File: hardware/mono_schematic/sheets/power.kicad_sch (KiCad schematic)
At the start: 37 parts

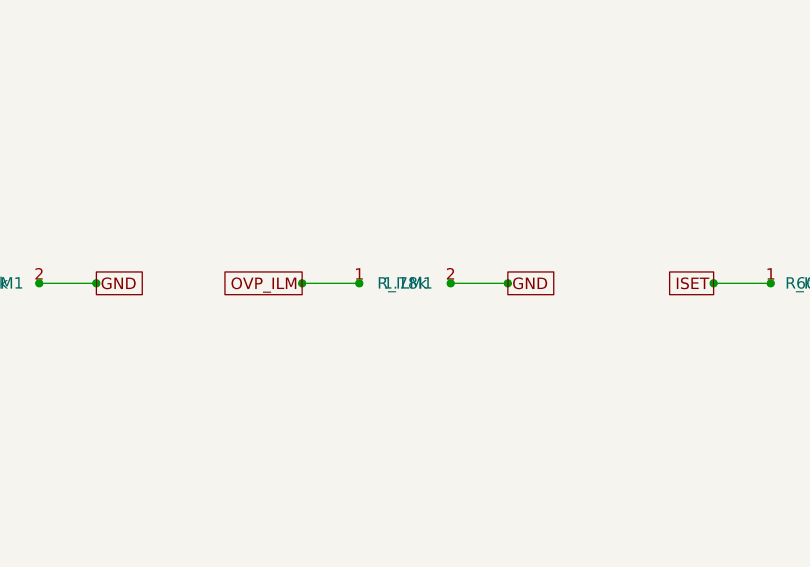
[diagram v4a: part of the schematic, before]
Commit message: mono_electronics v13 chunk4: abs-max review of every part; R_ILM1 1.78k->2.7k (eFuse limit 0.79 A < BQ25185 1.1 A IN abs max); schematic regen (ERC 0, 0 diffs)
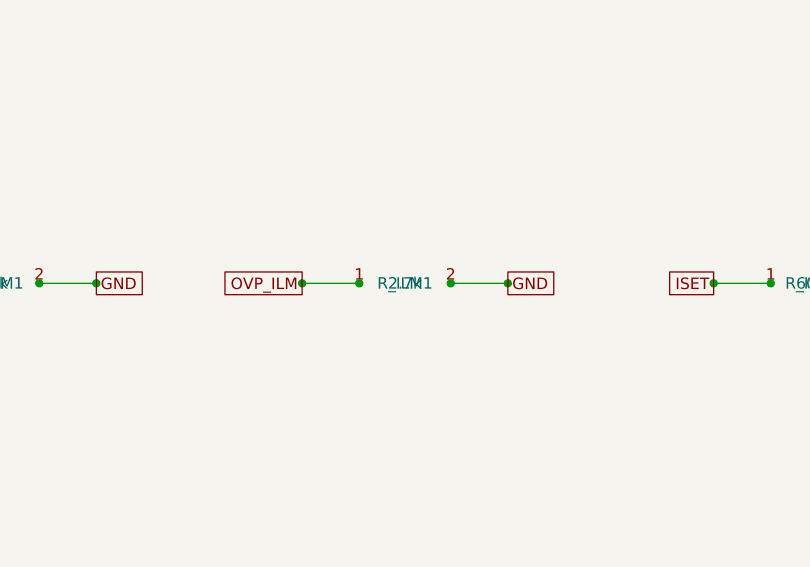
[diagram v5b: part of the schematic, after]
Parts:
- removed R_ILM1: 1.78k, mono_electronics:R_0402_1005Metric, symbol mono_parts:1.78k_R_0402_1005Metric_2
- added R_ILM1: 2.7k, mono_electronics:R_0402_1005Metric, symbol mono_parts:2.7k_R_0402_1005Metric_2
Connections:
- net GND: now also R_ILM1.2
- net OVP_ILM: now also R_ILM1.1
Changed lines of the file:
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@@
     (instances
       (project "mono_electronics"
-        (path "/45a3775a-69f2-487f-ba16-a63eb468321a"
+        (path "/f479e555-bc92-4042-8ffc-422502a71c2a"
           (reference "C_ASW_IN1")
           (unit 1)
@@
     (instances
       (project "mono_electronics"
-        (path "/45a3775a-69f2-487f-ba16-a63eb468321a"
+        (path "/f479e555-bc92-4042-8ffc-422502a71c2a"
           (reference "C_AUD_SW1")
           (unit 1)
@@
     (instances
       (project "mono_electronics"
-        (path "/45a3775a-69f2-487f-ba16-a63eb468321a"
+        (path "/f479e555-bc92-4042-8ffc-422502a71c2a"
           (reference "C_CHG_BAT1")
           (unit 1)
@@
     (instances
       (project "mono_electronics"
-        (path "/45a3775a-69f2-487f-ba16-a63eb468321a"
+        (path "/f479e555-bc92-4042-8ffc-422502a71c2a"
           (reference "C_CHG_IN1")
           (unit 1)
@@
     (instances
       (project "mono_electronics"
-        (path "/45a3775a-69f2-487f-ba16-a63eb468321a"
+        (path "/f479e555-bc92-4042-8ffc-422502a71c2a"
           (reference "C_CHG_SYS1")
           (unit 1)
@@
     (instances
       (project "mono_electronics"
-        (path "/45a3775a-69f2-487f-ba16-a63eb468321a"
+        (path "/f479e555-bc92-4042-8ffc-422502a71c2a"
           (reference "C_EN1")
           (unit 1)
@@
     (instances
       (project "mono_electronics"
-        (path "/45a3775a-69f2-487f-ba16-a63eb468321a"
+        (path "/f479e555-bc92-4042-8ffc-422502a71c2a"
           (reference "C_GAUGE1")
           (unit 1)
@@
     (instances
       (project "mono_electronics"
-        (path "/45a3775a-69f2-487f-ba16-a63eb468321a"
+        (path "/f479e555-bc92-4042-8ffc-422502a71c2a"
           (reference "C_LDO_IN1")
           (unit 1)
@@
     (instances
       (project "mono_electronics"
-        (path "/45a3775a-69f2-487f-ba16-a63eb468321a"
+        (path "/f479e555-bc92-4042-8ffc-422502a71c2a"
           (reference "C_LDO_OUT1")
           (unit 1)
@@
     (instances
       (project "mono_electronics"
-        (path "/45a3775a-69f2-487f-ba16-a63eb468321a"
+        (path "/f479e555-bc92-4042-8ffc-422502a71c2a"
           (reference "C_LED1")
           (unit 1)
@@
     (instances
       (project "mono_electronics"
-        (path "/45a3775a-69f2-487f-ba16-a63eb468321a"
+        (path "/f479e555-bc92-4042-8ffc-422502a71c2a"
           (reference "C_LED2")
           (unit 1)
@@
     (instances
       (project "mono_electronics"
-        (path "/45a3775a-69f2-487f-ba16-a63eb468321a"
+        (path "/f479e555-bc92-4042-8ffc-422502a71c2a"
           (reference "C_LL1")
           (unit 1)
@@
     (instances
       (project "mono_electronics"
-        (path "/45a3775a-69f2-487f-ba16-a63eb468321a"
+        (path "/f479e555-bc92-4042-8ffc-422502a71c2a"
           (reference "C_LL2")
           (unit 1)
@@
     (instances
       (project "mono_electronics"
-        (path "/45a3775a-69f2-487f-ba16-a63eb468321a"
+        (path "/f479e555-bc92-4042-8ffc-422502a71c2a"
           (reference "C_LL_IN1")
           (unit 1)
@@
     (instances
       (project "mono_electronics"
-        (path "/45a3775a-69f2-487f-ba16-a63eb468321a"
+        (path "/f479e555-bc92-4042-8ffc-422502a71c2a"
           (reference "C_SYS1")
           (unit 1)
@@
     (instances
       (project "mono_electronics"
-        (path "/45a3775a-69f2-487f-ba16-a63eb468321a"
+        (path "/f479e555-bc92-4042-8ffc-422502a71c2a"
           (reference "D_VBUS1")
           (unit 1)
@@
     (instances
       (project "mono_electronics"
-        (path "/45a3775a-69f2-487f-ba16-a63eb468321a"
+        (path "/f479e555-bc92-4042-8ffc-422502a71c2a"
           (reference "F_BAT1")
           (unit 1)
@@
     (instances
       (project "mono_electronics"
-        (path "/45a3775a-69f2-487f-ba16-a63eb468321a"
+        (path "/f479e555-bc92-4042-8ffc-422502a71c2a"
           (reference "J_BAT1")
           (unit 1)
@@
     (instances
       (project "mono_electronics"
-        (path "/45a3775a-69f2-487f-ba16-a63eb468321a"
+        (path "/f479e555-bc92-4042-8ffc-422502a71c2a"
           (reference "L_LED1")
           (unit 1)
@@
     (instances
       (project "mono_electronics"
-        (path "/45a3775a-69f2-487f-ba16-a63eb468321a"
+        (path "/f479e555-bc92-4042-8ffc-422502a71c2a"
           (reference "Q_BAT1")
           (unit 1)
@@
     (instances
       (project "mono_electronics"
-        (path "/45a3775a-69f2-487f-ba16-a63eb468321a"
+        (path "/f479e555-bc92-4042-8ffc-422502a71c2a"
           (reference "R_ALRT1")
           (unit 1)
@@
     (instances
       (project "mono_electronics"
-        (path "/45a3775a-69f2-487f-ba16-a63eb468321a"
+        (path "/f479e555-bc92-4042-8ffc-422502a71c2a"
           (reference "R_AUD_PD1")
           (unit 1)
@@
     (instances
       (project "mono_electronics"
-        (path "/45a3775a-69f2-487f-ba16-a63eb468321a"
+        (path "/f479e555-bc92-4042-8ffc-422502a71c2a"
           (reference "R_BATG1")
           (unit 1)
@@
     (instances
       (project "mono_electronics"
-        (path "/45a3775a-69f2-487f-ba16-a63eb468321a"
+        (path "/f479e555-bc92-4042-8ffc-422502a71c2a"
           (reference "R_FB_BOT1")
           (unit 1)
@@
     (instances
       (project "mono_electronics"
-        (path "/45a3775a-69f2-487f-ba16-a63eb468321a"
+        (path "/f479e555-bc92-4042-8ffc-422502a71c2a"
           (reference "R_FB_TOP1")
           (unit 1)
@@
     (instances
       (project "mono_electronics"
-        (path "/45a3775a-69f2-487f-ba16-a63eb468321a"
+        (path "/f479e555-bc92-4042-8ffc-422502a71c2a"
           (reference "R_ILIM1")
           (unit 1)
@@
   )
   (symbol
-    (lib_id "mono_parts:1.78k_R_0402_1005Metric_2")
+    (lib_id "mono_parts:2.7k_R_0402_1005Metric_2")
     (at 127 370.84 0)
     (unit 1)
@@
     (property
       "Value"
-      "1.78k"
+      "2.7k"
       (at 127 370.84 0)
       (effects
@@
     (instances
       (project "mono_electronics"
-        (path "/45a3775a-69f2-487f-ba16-a63eb468321a"
+        (path "/f479e555-bc92-4042-8ffc-422502a71c2a"
           (reference "R_ILM1")
           (unit 1)
@@
     (instances
       (project "mono_electronics"
-        (path "/45a3775a-69f2-487f-ba16-a63eb468321a"
+        (path "/f479e555-bc92-4042-8ffc-422502a71c2a"
           (reference "R_ISET1")
           (unit 1)
@@
     (instances
       (project "mono_electronics"
-        (path "/45a3775a-69f2-487f-ba16-a63eb468321a"
+        (path "/f479e555-bc92-4042-8ffc-422502a71c2a"
           (reference "R_LOGIC_PD1")
           (unit 1)
@@
     (instances
       (project "mono_electronics"
-        (path "/45a3775a-69f2-487f-ba16-a63eb468321a"
+        (path "/f479e555-bc92-4042-8ffc-422502a71c2a"
           (reference "R_QOD1")
           (unit 1)
@@
     (instances
       (project "mono_electronics"
-        (path "/45a3775a-69f2-487f-ba16-a63eb468321a"
+        (path "/f479e555-bc92-4042-8ffc-422502a71c2a"
           (reference "R_TH1")
           (unit 1)
@@
     (instances
       (project "mono_electronics"
-        (path "/45a3775a-69f2-487f-ba16-a63eb468321a"
+        (path "/f479e555-bc92-4042-8ffc-422502a71c2a"
           (reference "TH_PCB1")
           (unit 1)
@@
     (instances
       (project "mono_electronics"
-        (path "/45a3775a-69f2-487f-ba16-a63eb468321a"
+        (path "/f479e555-bc92-4042-8ffc-422502a71c2a"
           (reference "U_AUDIO_SW1")
           (unit 1)
@@
     (instances
       (project "mono_electronics"
-        (path "/45a3775a-69f2-487f-ba16-a63eb468321a"
+        (path "/f479e555-bc92-4042-8ffc-422502a71c2a"
           (reference "U_CHG1")
           (unit 1)
@@
     (instances
       (project "mono_electronics"
-        (path "/45a3775a-69f2-487f-ba16-a63eb468321a"
+        (path "/f479e555-bc92-4042-8ffc-422502a71c2a"
           (reference "U_GAUGE1")
           (unit 1)
@@
     (instances
       (project "mono_electronics"
-        (path "/45a3775a-69f2-487f-ba16-a63eb468321a"
+        (path "/f479e555-bc92-4042-8ffc-422502a71c2a"
           (reference "U_LDO1")
           (unit 1)
@@
     (instances
       (project "mono_electronics"
-        (path "/45a3775a-69f2-487f-ba16-a63eb468321a"
+        (path "/f479e555-bc92-4042-8ffc-422502a71c2a"
           (reference "U_OVP1")
           (unit 1)
@@
   )
   (sheet_instances
-    (path "/45a3775a-69f2-487f-ba16-a63eb468321a"
+    (path "/f479e555-bc92-4042-8ffc-422502a71c2a"
       (page "1")
     )

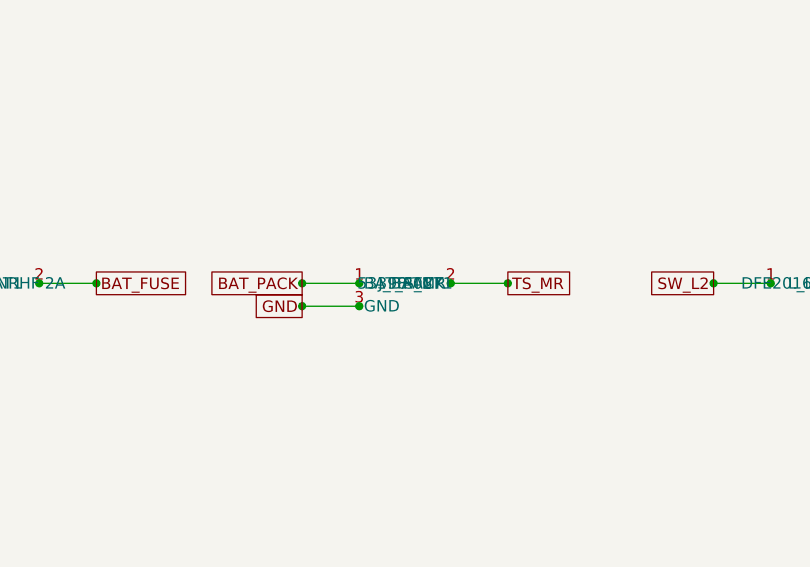
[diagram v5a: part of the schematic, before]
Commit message: mono_electronics v13b: J_BAT1 -> JST PH S3B-PH-SM4-TB (2 A/contact, C265101), battery path re-placed (1.0 mm BAT_PACK/BAT_FUSE/BAT_RAW), TS_MR rerouted; gates clean (DRC 0/0/0, ERC 0, 0 diffs, прозвонка 243/243); BOM stock/prices refreshed from JLC API; fab v13 regen
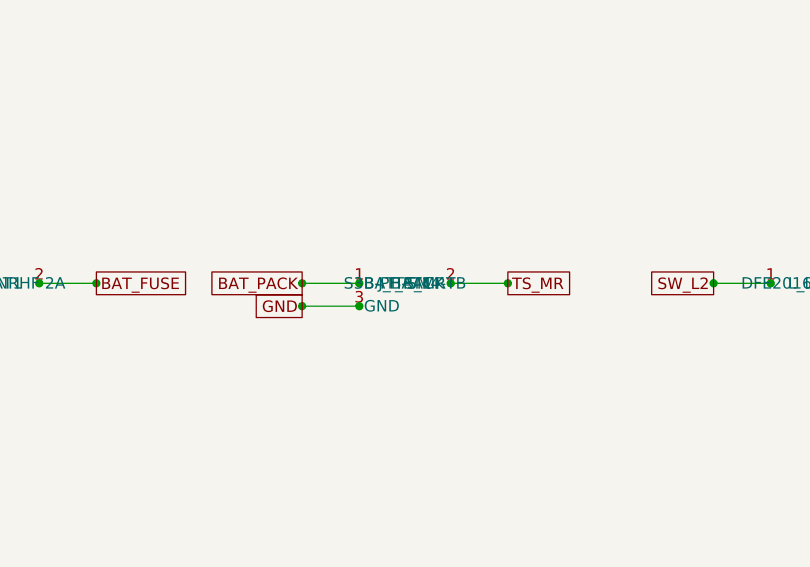
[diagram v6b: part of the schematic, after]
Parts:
- removed J_BAT1: 53398-0371, mono_electronics:Molex_PicoBlade_53398-0371_1x03-1MP_P1.25mm_Vertical, symbol mono_parts:53398-0371_Molex_PicoBlade_53398-0371_1x03-1MP_P1.25mm_Vertical_3
- added J_BAT1: S3B-PH-SM4-TB, mono_electronics:JST_PH_S3B-PH-SM4-TB_1x03-1MP_P2.00mm_Horizontal, symbol mono_parts:S3B-PH-SM4-TB_JST_PH_S3B-PH-SM4-TB_1x03-1MP_P2.00mm_Horizontal_3
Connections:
- net BAT_PACK: now also J_BAT1.1 (BAT_PACK)
- net GND: now also J_BAT1.3 (GND)
- net TS_MR: now also J_BAT1.2 (TS_MR)
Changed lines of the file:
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@@
     (instances
       (project "mono_electronics"
-        (path "/f479e555-bc92-4042-8ffc-422502a71c2a"
+        (path "/706eb51d-2e2a-47df-978e-c1eb7edb736e"
           (reference "C_ASW_IN1")
           (unit 1)
@@
     (instances
       (project "mono_electronics"
-        (path "/f479e555-bc92-4042-8ffc-422502a71c2a"
+        (path "/706eb51d-2e2a-47df-978e-c1eb7edb736e"
           (reference "C_AUD_SW1")
           (unit 1)
@@
     (instances
       (project "mono_electronics"
-        (path "/f479e555-bc92-4042-8ffc-422502a71c2a"
+        (path "/706eb51d-2e2a-47df-978e-c1eb7edb736e"
           (reference "C_CHG_BAT1")
           (unit 1)
@@
     (instances
       (project "mono_electronics"
-        (path "/f479e555-bc92-4042-8ffc-422502a71c2a"
+        (path "/706eb51d-2e2a-47df-978e-c1eb7edb736e"
           (reference "C_CHG_IN1")
           (unit 1)
@@
     (instances
       (project "mono_electronics"
-        (path "/f479e555-bc92-4042-8ffc-422502a71c2a"
+        (path "/706eb51d-2e2a-47df-978e-c1eb7edb736e"
           (reference "C_CHG_SYS1")
           (unit 1)
@@
     (instances
       (project "mono_electronics"
-        (path "/f479e555-bc92-4042-8ffc-422502a71c2a"
+        (path "/706eb51d-2e2a-47df-978e-c1eb7edb736e"
           (reference "C_EN1")
           (unit 1)
@@
     (instances
       (project "mono_electronics"
-        (path "/f479e555-bc92-4042-8ffc-422502a71c2a"
+        (path "/706eb51d-2e2a-47df-978e-c1eb7edb736e"
           (reference "C_GAUGE1")
           (unit 1)
@@
     (instances
       (project "mono_electronics"
-        (path "/f479e555-bc92-4042-8ffc-422502a71c2a"
+        (path "/706eb51d-2e2a-47df-978e-c1eb7edb736e"
           (reference "C_LDO_IN1")
           (unit 1)
@@
     (instances
       (project "mono_electronics"
-        (path "/f479e555-bc92-4042-8ffc-422502a71c2a"
+        (path "/706eb51d-2e2a-47df-978e-c1eb7edb736e"
           (reference "C_LDO_OUT1")
           (unit 1)
@@
     (instances
       (project "mono_electronics"
-        (path "/f479e555-bc92-4042-8ffc-422502a71c2a"
+        (path "/706eb51d-2e2a-47df-978e-c1eb7edb736e"
           (reference "C_LED1")
           (unit 1)
@@
     (instances
       (project "mono_electronics"
-        (path "/f479e555-bc92-4042-8ffc-422502a71c2a"
+        (path "/706eb51d-2e2a-47df-978e-c1eb7edb736e"
           (reference "C_LED2")
           (unit 1)
@@
     (instances
       (project "mono_electronics"
-        (path "/f479e555-bc92-4042-8ffc-422502a71c2a"
+        (path "/706eb51d-2e2a-47df-978e-c1eb7edb736e"
           (reference "C_LL1")
           (unit 1)
@@
     (instances
       (project "mono_electronics"
-        (path "/f479e555-bc92-4042-8ffc-422502a71c2a"
+        (path "/706eb51d-2e2a-47df-978e-c1eb7edb736e"
           (reference "C_LL2")
           (unit 1)
@@
     (instances
       (project "mono_electronics"
-        (path "/f479e555-bc92-4042-8ffc-422502a71c2a"
+        (path "/706eb51d-2e2a-47df-978e-c1eb7edb736e"
           (reference "C_LL_IN1")
           (unit 1)
@@
     (instances
       (project "mono_electronics"
-        (path "/f479e555-bc92-4042-8ffc-422502a71c2a"
+        (path "/706eb51d-2e2a-47df-978e-c1eb7edb736e"
           (reference "C_SYS1")
           (unit 1)
@@
     (instances
       (project "mono_electronics"
-        (path "/f479e555-bc92-4042-8ffc-422502a71c2a"
+        (path "/706eb51d-2e2a-47df-978e-c1eb7edb736e"
           (reference "D_VBUS1")
           (unit 1)
@@
     (instances
       (project "mono_electronics"
-        (path "/f479e555-bc92-4042-8ffc-422502a71c2a"
+        (path "/706eb51d-2e2a-47df-978e-c1eb7edb736e"
           (reference "F_BAT1")
           (unit 1)
@@
   )
   (symbol
-    (lib_id "mono_parts:53398-0371_Molex_PicoBlade_53398-0371_1x03-1MP_P1.25mm_Vertical_3")
+    (lib_id "mono_parts:S3B-PH-SM4-TB_JST_PH_S3B-PH-SM4-TB_1x03-1MP_P2.00mm_Horizontal_3")
     (at 81.28 259.08 0)
     (unit 1)
@@
     (property
       "Value"
-      "53398-0371"
+      "S3B-PH-SM4-TB"
       (at 81.28 259.08 0)
       (effects
@@
     (property
       "Footprint"
-      "mono_electronics:Molex_PicoBlade_53398-0371_1x03-1MP_P1.25mm_Vertical"
+      "mono_electronics:JST_PH_S3B-PH-SM4-TB_1x03-1MP_P2.00mm_Horizontal"
       (at 81.28 259.08 0)
       (effects
@@
     (instances
       (project "mono_electronics"
-        (path "/f479e555-bc92-4042-8ffc-422502a71c2a"
+        (path "/706eb51d-2e2a-47df-978e-c1eb7edb736e"
           (reference "J_BAT1")
           (unit 1)
@@
     (instances
       (project "mono_electronics"
-        (path "/f479e555-bc92-4042-8ffc-422502a71c2a"
+        (path "/706eb51d-2e2a-47df-978e-c1eb7edb736e"
           (reference "L_LED1")
           (unit 1)
@@
     (instances
       (project "mono_electronics"
-        (path "/f479e555-bc92-4042-8ffc-422502a71c2a"
+        (path "/706eb51d-2e2a-47df-978e-c1eb7edb736e"
           (reference "Q_BAT1")
           (unit 1)
@@
     (instances
       (project "mono_electronics"
-        (path "/f479e555-bc92-4042-8ffc-422502a71c2a"
+        (path "/706eb51d-2e2a-47df-978e-c1eb7edb736e"
           (reference "R_ALRT1")
           (unit 1)
@@
     (instances
       (project "mono_electronics"
-        (path "/f479e555-bc92-4042-8ffc-422502a71c2a"
+        (path "/706eb51d-2e2a-47df-978e-c1eb7edb736e"
           (reference "R_AUD_PD1")
           (unit 1)
@@
     (instances
       (project "mono_electronics"
-        (path "/f479e555-bc92-4042-8ffc-422502a71c2a"
+        (path "/706eb51d-2e2a-47df-978e-c1eb7edb736e"
           (reference "R_BATG1")
           (unit 1)
@@
     (instances
       (project "mono_electronics"
-        (path "/f479e555-bc92-4042-8ffc-422502a71c2a"
+        (path "/706eb51d-2e2a-47df-978e-c1eb7edb736e"
           (reference "R_FB_BOT1")
           (unit 1)
@@
     (instances
       (project "mono_electronics"
-        (path "/f479e555-bc92-4042-8ffc-422502a71c2a"
+        (path "/706eb51d-2e2a-47df-978e-c1eb7edb736e"
           (reference "R_FB_TOP1")
           (unit 1)
@@
     (instances
       (project "mono_electronics"
-        (path "/f479e555-bc92-4042-8ffc-422502a71c2a"
+        (path "/706eb51d-2e2a-47df-978e-c1eb7edb736e"
           (reference "R_ILIM1")
           (unit 1)
@@
     (instances
       (project "mono_electronics"
-        (path "/f479e555-bc92-4042-8ffc-422502a71c2a"
+        (path "/706eb51d-2e2a-47df-978e-c1eb7edb736e"
           (reference "R_ILM1")
           (unit 1)
@@
     (instances
       (project "mono_electronics"
-        (path "/f479e555-bc92-4042-8ffc-422502a71c2a"
+        (path "/706eb51d-2e2a-47df-978e-c1eb7edb736e"
           (reference "R_ISET1")
           (unit 1)
@@
     (instances
       (project "mono_electronics"
-        (path "/f479e555-bc92-4042-8ffc-422502a71c2a"
+        (path "/706eb51d-2e2a-47df-978e-c1eb7edb736e"
           (reference "R_LOGIC_PD1")
           (unit 1)
@@
     (instances
       (project "mono_electronics"
-        (path "/f479e555-bc92-4042-8ffc-422502a71c2a"
+        (path "/706eb51d-2e2a-47df-978e-c1eb7edb736e"
           (reference "R_QOD1")
           (unit 1)
@@
     (instances
       (project "mono_electronics"
-        (path "/f479e555-bc92-4042-8ffc-422502a71c2a"
+        (path "/706eb51d-2e2a-47df-978e-c1eb7edb736e"
           (reference "R_TH1")
           (unit 1)
@@
     (instances
       (project "mono_electronics"
-        (path "/f479e555-bc92-4042-8ffc-422502a71c2a"
+        (path "/706eb51d-2e2a-47df-978e-c1eb7edb736e"
           (reference "TH_PCB1")
           (unit 1)
@@
     (instances
       (project "mono_electronics"
-        (path "/f479e555-bc92-4042-8ffc-422502a71c2a"
+        (path "/706eb51d-2e2a-47df-978e-c1eb7edb736e"
           (reference "U_AUDIO_SW1")
           (unit 1)
@@
     (instances
       (project "mono_electronics"
-        (path "/f479e555-bc92-4042-8ffc-422502a71c2a"
+        (path "/706eb51d-2e2a-47df-978e-c1eb7edb736e"
           (reference "U_CHG1")
           (unit 1)
@@
     (instances
       (project "mono_electronics"
-        (path "/f479e555-bc92-4042-8ffc-422502a71c2a"
+        (path "/706eb51d-2e2a-47df-978e-c1eb7edb736e"
           (reference "U_GAUGE1")
           (unit 1)
@@
     (instances
       (project "mono_electronics"
-        (path "/f479e555-bc92-4042-8ffc-422502a71c2a"
+        (path "/706eb51d-2e2a-47df-978e-c1eb7edb736e"
           (reference "U_LDO1")
           (unit 1)
@@
     (instances
       (project "mono_electronics"
-        (path "/f479e555-bc92-4042-8ffc-422502a71c2a"
+        (path "/706eb51d-2e2a-47df-978e-c1eb7edb736e"
           (reference "U_OVP1")
           (unit 1)
@@
   )
   (sheet_instances
-    (path "/f479e555-bc92-4042-8ffc-422502a71c2a"
+    (path "/706eb51d-2e2a-47df-978e-c1eb7edb736e"
       (page "1")
     )
